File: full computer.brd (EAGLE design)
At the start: 99.6 x 90.2 mm, 74 parts, among them IC2 74HC541N, IC3 74HC573N, IC4 74HC04N, Q1 IRF9530, X1 1503_08

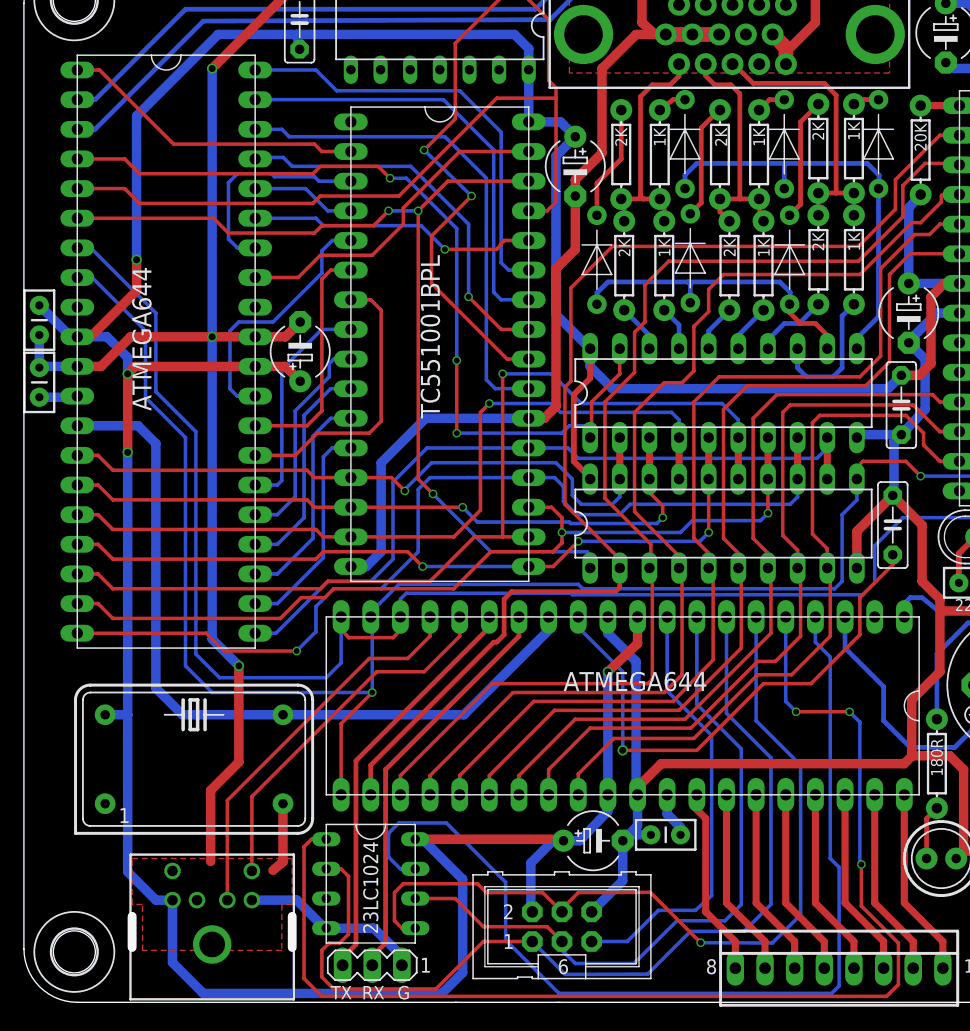
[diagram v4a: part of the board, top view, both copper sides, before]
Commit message: added test pads for H anv V sync signals
Signed-off-by: Panagiotis Varelas <varelaspanos@gmail.com>
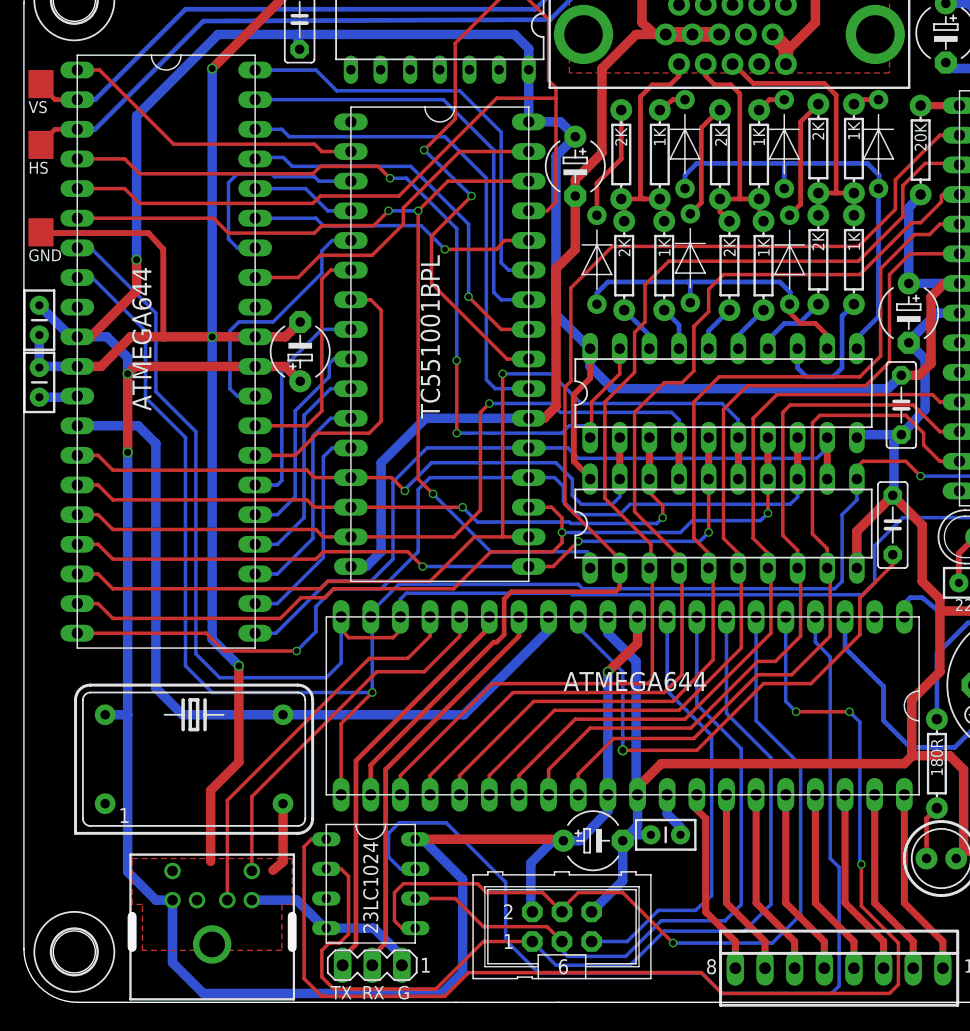
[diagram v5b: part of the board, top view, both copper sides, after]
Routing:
- net GND: track 521.5 -> 539.2 mm
- net N$46: track 0.00 -> 1.61 mm
- net N$62: track 0.00 -> 1.48 mm
- net N$52: track 103.6 -> 105.1 mm
- net N$50: track 82.7 -> 82.1 mm
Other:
- board text added: "GND"
- board text added: "HS"
- board text added: "VS"
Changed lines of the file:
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@@
 <wire x1="104.648" y1="91.821" x2="104.648" y2="94.234" width="0.2032" layer="22" style="shortdash"/>
 <wire x1="104.648" y1="94.234" x2="102.235" y2="94.234" width="0.2032" layer="22" style="shortdash"/>
+<rectangle x1="39.624" y1="74.93" x2="41.783" y2="77.343" layer="1"/>
 <rectangle x1="39.497" y1="74.803" x2="41.91" y2="77.47" layer="29"/>
+<rectangle x1="39.624" y1="82.423" x2="41.783" y2="84.836" layer="1"/>
 <rectangle x1="39.497" y1="82.296" x2="41.91" y2="84.963" layer="29"/>
+<rectangle x1="39.624" y1="87.63" x2="41.783" y2="90.043" layer="1"/>
 <rectangle x1="39.497" y1="87.503" x2="41.91" y2="90.17" layer="29"/>
+<text x="39.624" y="86.36" size="1.016" layer="25">VS</text>
+<text x="39.624" y="81.153" size="1.016" layer="25">HS</text>
+<text x="39.624" y="73.66" size="1.016" layer="25">GND</text>
 <wire x1="129.286" y1="88.265" x2="129.286" y2="57.277" width="0.254" layer="22" style="shortdash"/>
 <wire x1="138.303" y1="57.277" x2="138.176" y2="88.265" width="0.254" layer="22" style="shortdash"/>
@@
 <wire x1="96.901" y1="35.687" x2="100.711" y2="31.877" width="0.3048" layer="16"/>
 <wire x1="100.711" y1="31.877" x2="100.711" y2="18.542" width="0.3048" layer="16"/>
-<wire x1="99.314" y1="17.145" x2="95.1992" y2="17.145" width="0.3048" layer="16"/>
-<wire x1="95.1992" y1="17.145" x2="91.5162" y2="13.4874" width="0.3048" layer="16"/>
-<wire x1="91.5162" y1="13.4874" x2="86.487" y2="13.4874" width="0.3048" layer="16"/>
-<wire x1="86.487" y1="13.4874" x2="85.344" y2="14.605" width="0.3048" layer="16"/>
+<wire x1="99.314" y1="17.145" x2="93.853" y2="17.145" width="0.3048" layer="16"/>
+<wire x1="93.853" y1="17.145" x2="90.805" y2="14.097" width="0.3048" layer="16"/>
+<wire x1="90.805" y1="14.097" x2="85.852" y2="14.097" width="0.3048" layer="16"/>
+<wire x1="85.852" y1="14.097" x2="85.344" y2="14.605" width="0.3048" layer="16"/>
 <wire x1="85.344" y1="14.605" x2="85.344" y2="15.367" width="0.3048" layer="16"/>
 <wire x1="99.314" y1="17.145" x2="100.711" y2="18.542" width="0.3048" layer="16"/>
@@
 <contactref element="U$10" pad="SO"/>
 <contactref element="ISP" pad="1"/>
-<wire x1="82.804" y1="15.367" x2="85.6234" y2="12.5476" width="0.3048" layer="16"/>
-<wire x1="85.6234" y1="12.5476" x2="92.6846" y2="12.573" width="0.3048" layer="16"/>
-<wire x1="92.6846" y1="12.573" x2="96.3422" y2="16.2306" width="0.3048" layer="16"/>
+<wire x1="82.804" y1="15.367" x2="84.836" y2="13.335" width="0.3048" layer="16"/>
+<wire x1="84.836" y1="13.335" x2="91.186" y2="13.335" width="0.3048" layer="16"/>
+<wire x1="91.186" y1="13.335" x2="94.107" y2="16.256" width="0.3048" layer="16"/>
 <wire x1="103.251" y1="18.542" x2="103.251" y2="31.115" width="0.3048" layer="16"/>
 <wire x1="103.251" y1="31.115" x2="99.441" y2="34.925" width="0.3048" layer="16"/>
 <wire x1="99.441" y1="34.925" x2="99.441" y2="43.18" width="0.3048" layer="16"/>
-<wire x1="96.3422" y1="16.2306" x2="100.965" y2="16.256" width="0.3048" layer="16"/>
+<wire x1="94.107" y1="16.256" x2="100.965" y2="16.256" width="0.3048" layer="16"/>
 <wire x1="100.965" y1="16.256" x2="103.251" y2="18.542" width="0.3048" layer="16"/>
 <wire x1="82.804" y1="15.367" x2="78.613" y2="15.367" width="0.3048" layer="1"/>
@@
 <contactref element="U$1" pad="PB5"/>
 <contactref element="ISP" pad="4"/>
-<wire x1="92.9132" y1="19.5834" x2="97.2312" y2="15.2654" width="0.3048" layer="1"/>
-<via x="97.2312" y="15.2654" extent="1-16" drill="0.5" shape="octagon"/>
+<wire x1="90.551" y1="19.558" x2="94.869" y2="15.24" width="0.3048" layer="1"/>
+<via x="94.869" y="15.24" extent="1-16" drill="0.5" shape="octagon"/>
 <wire x1="105.791" y1="17.653" x2="105.791" y2="30.48" width="0.3048" layer="16"/>
 <wire x1="105.791" y1="30.48" x2="101.981" y2="34.29" width="0.3048" layer="16"/>
 <wire x1="101.981" y1="34.29" x2="101.981" y2="43.18" width="0.3048" layer="16"/>
-<wire x1="92.9132" y1="19.5834" x2="86.741" y2="19.558" width="0.3048" layer="1"/>
+<wire x1="90.551" y1="19.558" x2="86.741" y2="19.558" width="0.3048" layer="1"/>
 <wire x1="86.741" y1="19.558" x2="85.344" y2="18.161" width="0.3048" layer="1"/>
 <wire x1="85.344" y1="18.161" x2="85.344" y2="17.907" width="0.3048" layer="1"/>
 <wire x1="105.791" y1="17.653" x2="103.378" y2="15.24" width="0.3048" layer="16"/>
-<wire x1="103.378" y1="15.24" x2="97.2312" y2="15.2654" width="0.3048" layer="16"/>
+<wire x1="103.378" y1="15.24" x2="94.869" y2="15.24" width="0.3048" layer="16"/>
 <wire x1="72.771" y1="16.51" x2="71.628" y2="16.51" width="0.3048" layer="1"/>
 <wire x1="71.628" y1="16.51" x2="70.993" y2="17.145" width="0.3048" layer="1"/>
@@
 <contactref element="U$1" pad="PB4"/>
 <contactref element="U$10" pad="~CS"/>
-<wire x1="113.411" y1="10.922" x2="113.8936" y2="11.4046" width="0.3048" layer="1"/>
-<wire x1="113.8936" y1="11.4046" x2="114.173" y2="11.684" width="0.3048" layer="1"/>
+<wire x1="77.343" y1="12.7" x2="97.282" y2="12.7" width="0.3048" layer="1"/>
+<wire x1="97.282" y1="12.7" x2="99.06" y2="10.922" width="0.3048" layer="1"/>
+<wire x1="99.06" y1="10.922" x2="113.411" y2="10.922" width="0.3048" layer="1"/>
+<wire x1="113.411" y1="10.922" x2="114.173" y2="11.684" width="0.3048" layer="1"/>
 <wire x1="114.173" y1="11.684" x2="114.173" y2="15.24" width="0.3048" layer="1"/>
 <wire x1="114.173" y1="15.24" x2="110.998" y2="18.415" width="0.3048" layer="1"/>
@@
 <wire x1="105.41" y1="35.052" x2="104.521" y2="35.941" width="0.3048" layer="16"/>
 <wire x1="104.521" y1="35.941" x2="104.521" y2="43.18" width="0.3048" layer="16"/>
+<wire x1="77.343" y1="12.7" x2="75.311" y2="10.668" width="0.3048" layer="1"/>
+<wire x1="75.311" y1="10.668" x2="64.77" y2="10.668" width="0.3048" layer="1"/>
 <wire x1="64.77" y1="10.668" x2="63.246" y2="12.192" width="0.3048" layer="1"/>
 <wire x1="63.246" y1="12.192" x2="63.246" y2="23.495" width="0.3048" layer="1"/>
 <wire x1="63.246" y1="23.495" x2="63.881" y2="24.13" width="0.3048" layer="1"/>
 <wire x1="63.881" y1="24.13" x2="65.151" y2="24.13" width="0.3048" layer="1"/>
-<wire x1="64.77" y1="10.668" x2="113.157" y2="10.668" width="0.3048" layer="1"/>
-<wire x1="113.157" y1="10.668" x2="113.411" y2="10.922" width="0.3048" layer="1"/>
 </signal>
 <signal name="N$53">
@@
 <contactref element="U$1" pad="PB3"/>
 <wire x1="80.518" y1="20.447" x2="80.518" y2="15.494" width="0.3048" layer="16"/>
-<wire x1="80.518" y1="15.494" x2="85.09" y2="10.922" width="0.3048" layer="16"/>
-<wire x1="85.09" y1="10.922" x2="108.458" y2="10.922" width="0.3048" layer="16"/>
+<wire x1="80.518" y1="15.494" x2="83.312" y2="12.7" width="0.3048" layer="16"/>
+<wire x1="83.312" y1="12.7" x2="97.282" y2="12.7" width="0.3048" layer="16"/>
+<wire x1="97.282" y1="12.7" x2="99.06" y2="10.922" width="0.3048" layer="16"/>
+<wire x1="99.06" y1="10.922" x2="108.458" y2="10.922" width="0.3048" layer="16"/>
 <wire x1="108.458" y1="10.922" x2="109.093" y2="11.557" width="0.3048" layer="16"/>
 <wire x1="109.093" y1="11.557" x2="109.093" y2="21.717" width="0.3048" layer="16"/>
@@
 <wire x1="90.932" y1="15.367" x2="87.884" y2="15.367" width="0.3048" layer="16"/>
 </signal>
+<signal name="N$46">
+<wire x1="42.799" y1="87.503" x2="41.91" y2="87.503" width="0.4064" layer="1"/>
+<wire x1="41.91" y1="87.503" x2="41.402" y2="88.011" width="0.4064" layer="1"/>
+</signal>
+<signal name="N$62">
+<wire x1="42.672" y1="84.963" x2="41.91" y2="84.963" width="0.4064" layer="1"/>
+<wire x1="41.91" y1="84.963" x2="41.402" y2="84.455" width="0.4064" layer="1"/>
+</signal>
 <signal name="N$66">
 </signal>
@@
 <vertex x="85.979" y="99.822"/>
 </polygon>
+<wire x1="41.656" y1="76.073" x2="49.911" y2="76.073" width="0.508" layer="1"/>
+<wire x1="49.911" y1="76.073" x2="51.181" y2="74.676" width="0.508" layer="1"/>
 <contactref element="IC2" pad="10"/>
 <contactref element="IC3" pad="10"/>
@@
 <wire x1="61.6458" y1="67.183" x2="62.9158" y2="68.453" width="0.8128" layer="1"/>
 <wire x1="124.333" y1="71.755" x2="127.0254" y2="71.755" width="0.8128" layer="1"/>
-<wire x1="55.372" y1="67.183" x2="48.387" y2="67.183" width="0.8128" layer="1"/>
+<wire x1="55.372" y1="67.183" x2="51.181" y2="67.183" width="0.8128" layer="1"/>
+<wire x1="51.181" y1="67.183" x2="48.387" y2="67.183" width="0.8128" layer="1"/>
 <wire x1="48.387" y1="67.183" x2="45.847" y2="64.643" width="0.8128" layer="1"/>
 <wire x1="45.847" y1="64.643" x2="43.815" y2="64.643" width="0.8128" layer="1"/>
@@
 <wire x1="96.525" y1="93.091" x2="98.815" y2="93.091" width="1.27" layer="1"/>
 <wire x1="93.853" y1="93.091" x2="94.235" y2="93.091" width="0.8128" layer="1"/>
+<wire x1="51.181" y1="74.676" x2="51.181" y2="67.183" width="0.508" layer="1"/>
 <wire x1="55.372" y1="41.275" x2="57.658" y2="38.989" width="0.8128" layer="16"/>
 <contactref element="D1" pad="K"/>
